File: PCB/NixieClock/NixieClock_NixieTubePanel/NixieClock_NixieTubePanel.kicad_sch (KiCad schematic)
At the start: 31 parts, among them J3 Conn_01x04_Pin, J4 Conn_01x04_Pin, U1 K155ID1, U2 K155ID1, U3 K155ID1, U4 K155ID1, U5 PCF8574, U6 PCF8574, X1 5230, X2 5230, X3 5230, X4 5230, X5 5230, X6 5230

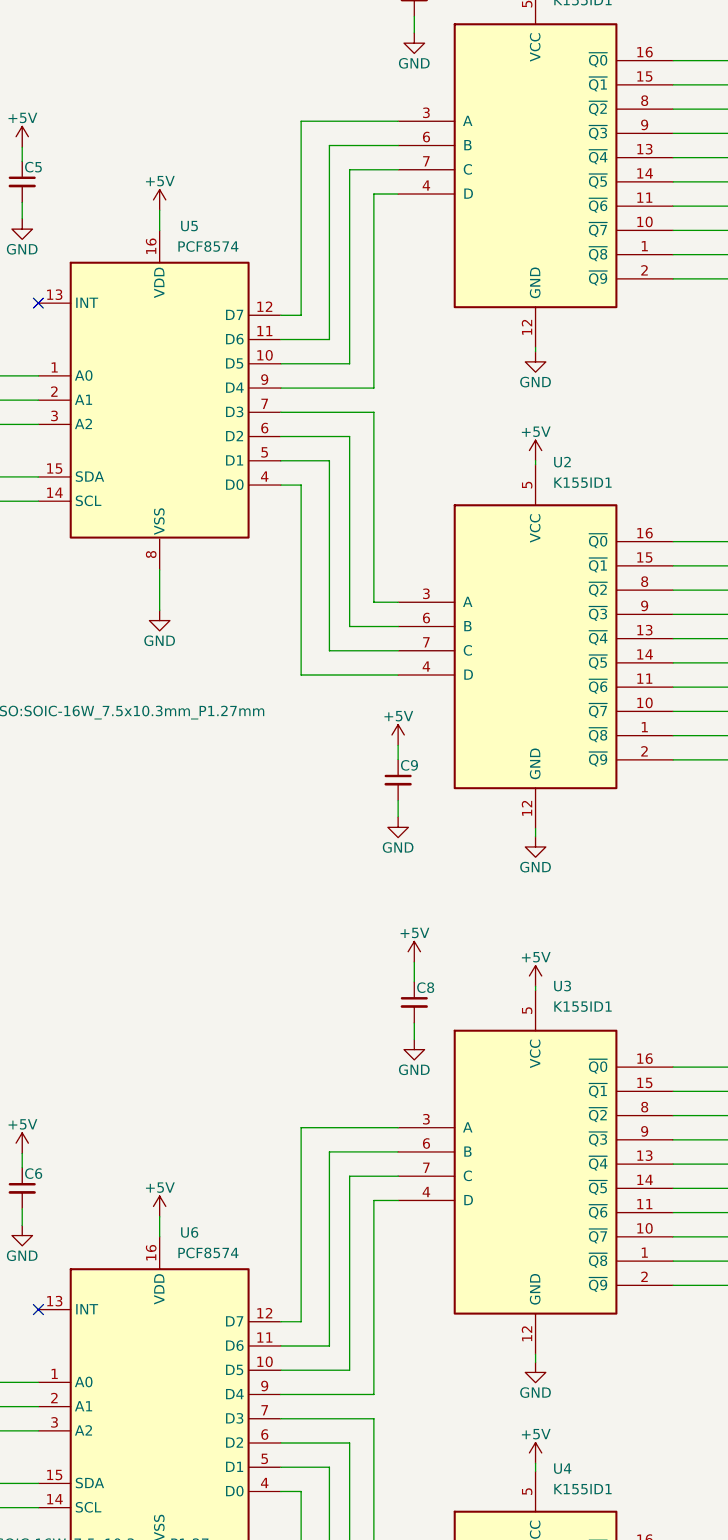
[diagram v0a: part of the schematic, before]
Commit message: Tidied U1 and U3 connections
adjust pin ordering on U1 and U3 in schematic so they would connect to the PCF chips neater on the PCB without needing vias
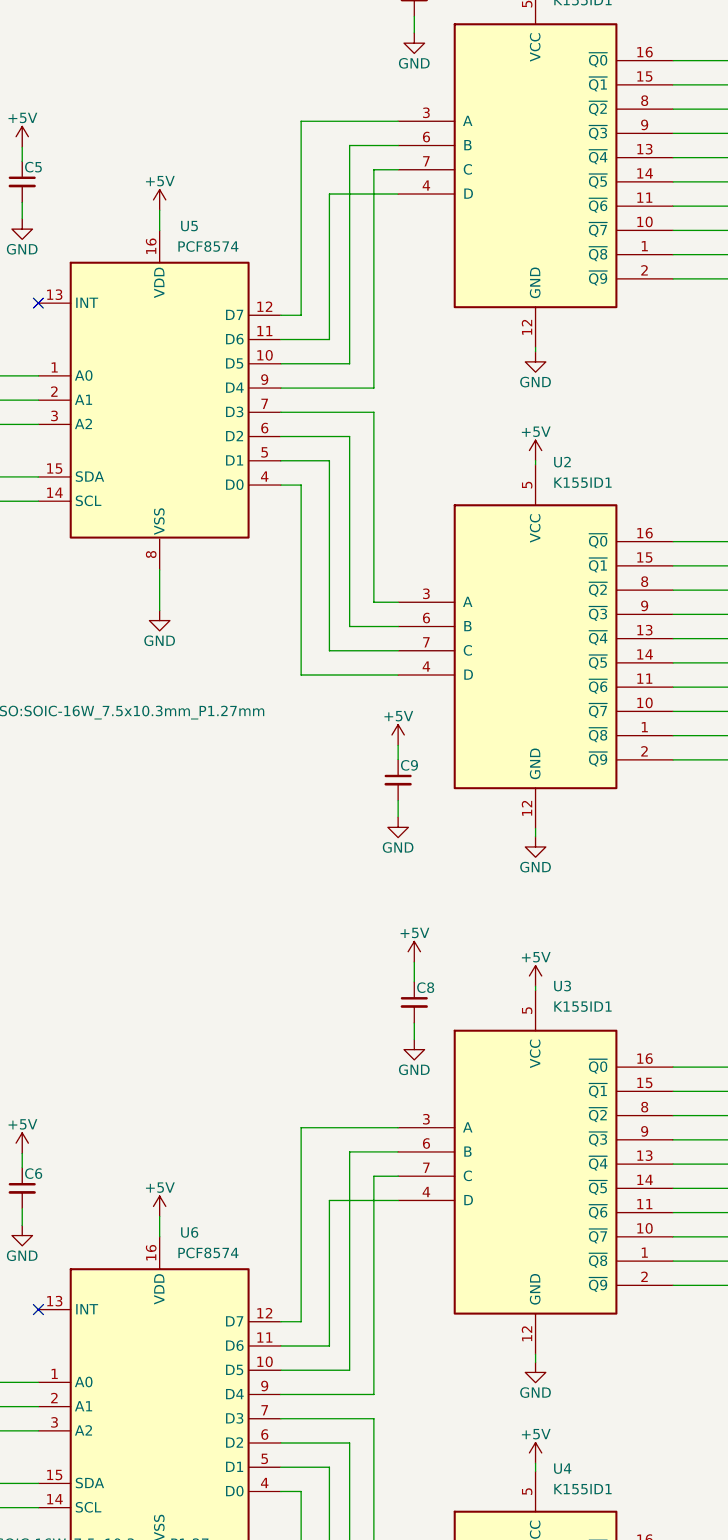
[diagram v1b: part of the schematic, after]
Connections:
- net at U5.10 (D5): now also U1.6 (B); no longer U1.7 (C)
- net at U5.11 (D6): now also U1.4 (D); no longer U1.6 (B)
- net at U5.9 (D4): now also U1.7 (C); no longer U1.4 (D)
- net at U3.4 (D): now also U6.11 (D6); no longer U6.9 (D4)
- net at U3.6 (B): now also U6.10 (D5); no longer U6.11 (D6)
- net at U3.7 (C): now also U6.9 (D4); no longer U6.10 (D5)
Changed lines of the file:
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@@
-	(wire
-		(pts
-			(xy 170 55) (xy 170 79)
-		)
-		(stroke
-			(width 0)
-			(type default)
-		)
-	)
 	(wire
 		(pts
@@
 	(wire
 		(pts
-			(xy 167.5 52) (xy 176 52)
-		)
-		(stroke
-			(width 0)
-			(type default)
-		)
-	)
-	(wire
-		(pts
 			(xy 35 261) (xy 35 262.5)
 		)
@@
 	(wire
 		(pts
-			(xy 173 82) (xy 173 58)
+			(xy 173 55) (xy 173 82)
 		)
 		(stroke
@@
 	(wire
 		(pts
-			(xy 167.5 200.5) (xy 167.5 176.5)
+			(xy 167.5 200.5) (xy 167.5 182.5)
 		)
 		(stroke
@@
 	(wire
 		(pts
+			(xy 170 52) (xy 176 52)
+		)
+		(stroke
+			(width 0)
+			(type default)
+		)
+	)
+	(wire
+		(pts
 			(xy 146.5 60) (xy 146.5 62.5)
 		)
@@
 	(wire
 		(pts
+			(xy 170 176.5) (xy 176 176.5)
+		)
+		(stroke
+			(width 0)
+			(type default)
+		)
+	)
+	(wire
+		(pts
 			(xy 232.5 172) (xy 232.5 164.5)
 		)
@@
 	(wire
 		(pts
-			(xy 167.5 76) (xy 167.5 52)
+			(xy 167.5 76) (xy 167.5 58)
 		)
 		(stroke
@@
 	(wire
 		(pts
-			(xy 170 179.5) (xy 170 203.5)
+			(xy 170 176.5) (xy 170 203.5)
 		)
 		(stroke
@@
 	(wire
 		(pts
+			(xy 176 179.5) (xy 173 179.5)
+		)
+		(stroke
+			(width 0)
+			(type default)
+		)
+	)
+	(wire
+		(pts
 			(xy 260 188) (xy 260 194.5)
 		)
@@
 	(wire
 		(pts
-			(xy 176 179.5) (xy 170 179.5)
-		)
-		(stroke
-			(width 0)
-			(type default)
-		)
-	)
-	(wire
-		(pts
 			(xy 255 251.5) (xy 255 247.5)
 		)
@@
 	(wire
 		(pts
+			(xy 170 52) (xy 170 79)
+		)
+		(stroke
+			(width 0)
+			(type default)
+		)
+	)
+	(wire
+		(pts
 			(xy 235.5 103) (xy 245.5 103)
 		)
@@
 	(wire
 		(pts
-			(xy 173 182.5) (xy 176 182.5)
-		)
-		(stroke
-			(width 0)
-			(type default)
-		)
-	)
-	(wire
-		(pts
 			(xy 69 166.5) (xy 69 160.54)
 		)
@@
 	(wire
 		(pts
-			(xy 173 58) (xy 176 58)
-		)
-		(stroke
-			(width 0)
-			(type default)
-		)
-	)
-	(wire
-		(pts
 			(xy 21 274) (xy 21 275.5)
 		)
@@
 	(wire
 		(pts
+			(xy 167.5 182.5) (xy 176 182.5)
+		)
+		(stroke
+			(width 0)
+			(type default)
+		)
+	)
+	(wire
+		(pts
 			(xy 260 35) (xy 260 43.5)
 		)
@@
 	(wire
 		(pts
+			(xy 173 55) (xy 176 55)
+		)
+		(stroke
+			(width 0)
+			(type default)
+		)
+	)
+	(wire
+		(pts
 			(xy 178 36.04) (xy 178 38.072)
 		)
@@
 	(wire
 		(pts
+			(xy 167.5 58) (xy 176 58)
+		)
+		(stroke
+			(width 0)
+			(type default)
+		)
+	)
+	(wire
+		(pts
 			(xy 43.5 27.54) (xy 43.5 30.19)
 		)
@@
 	(wire
 		(pts
-			(xy 176 55) (xy 170 55)
-		)
-		(stroke
-			(width 0)
-			(type default)
-		)
-	)
-	(wire
-		(pts
 			(xy 173 209.5) (xy 173 233)
 		)
@@
 	(wire
 		(pts
-			(xy 173 206.5) (xy 173 182.5)
+			(xy 173 179.5) (xy 173 206.5)
 		)
 		(stroke
@@
 		)
 		(stroke
-			(width 0)
-			(type default)
-		)
-	)
-	(wire
-		(pts
-			(xy 167.5 176.5) (xy 176 176.5)
-		)
-		(stroke

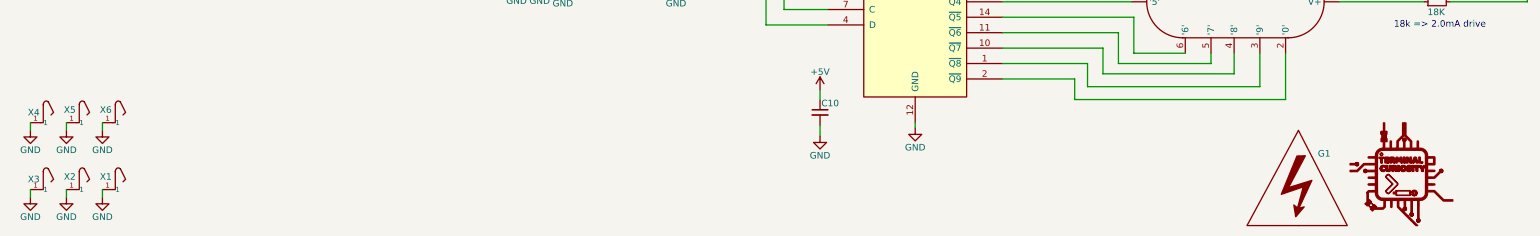
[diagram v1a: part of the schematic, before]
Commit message: DRC cleared
0 DRC errors
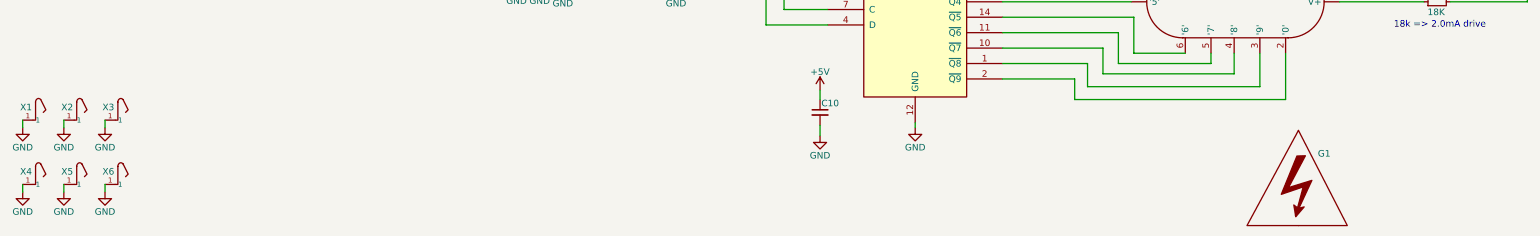
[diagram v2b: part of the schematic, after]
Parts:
- removed G2: LOGO, TerminalCuriosityFootprints:LABEL_TerminalCuriosity_25.0x25.0mm, symbol TerminalCuriosityLogo:LOGO
- N1, N2, N3, N4: footprint TerminalCuriosityFootprints:in-12_nixie-tube -> TerminalCuriosityFootprints:in-12_nixie-tube-socket
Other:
- moved on the sheet: X1

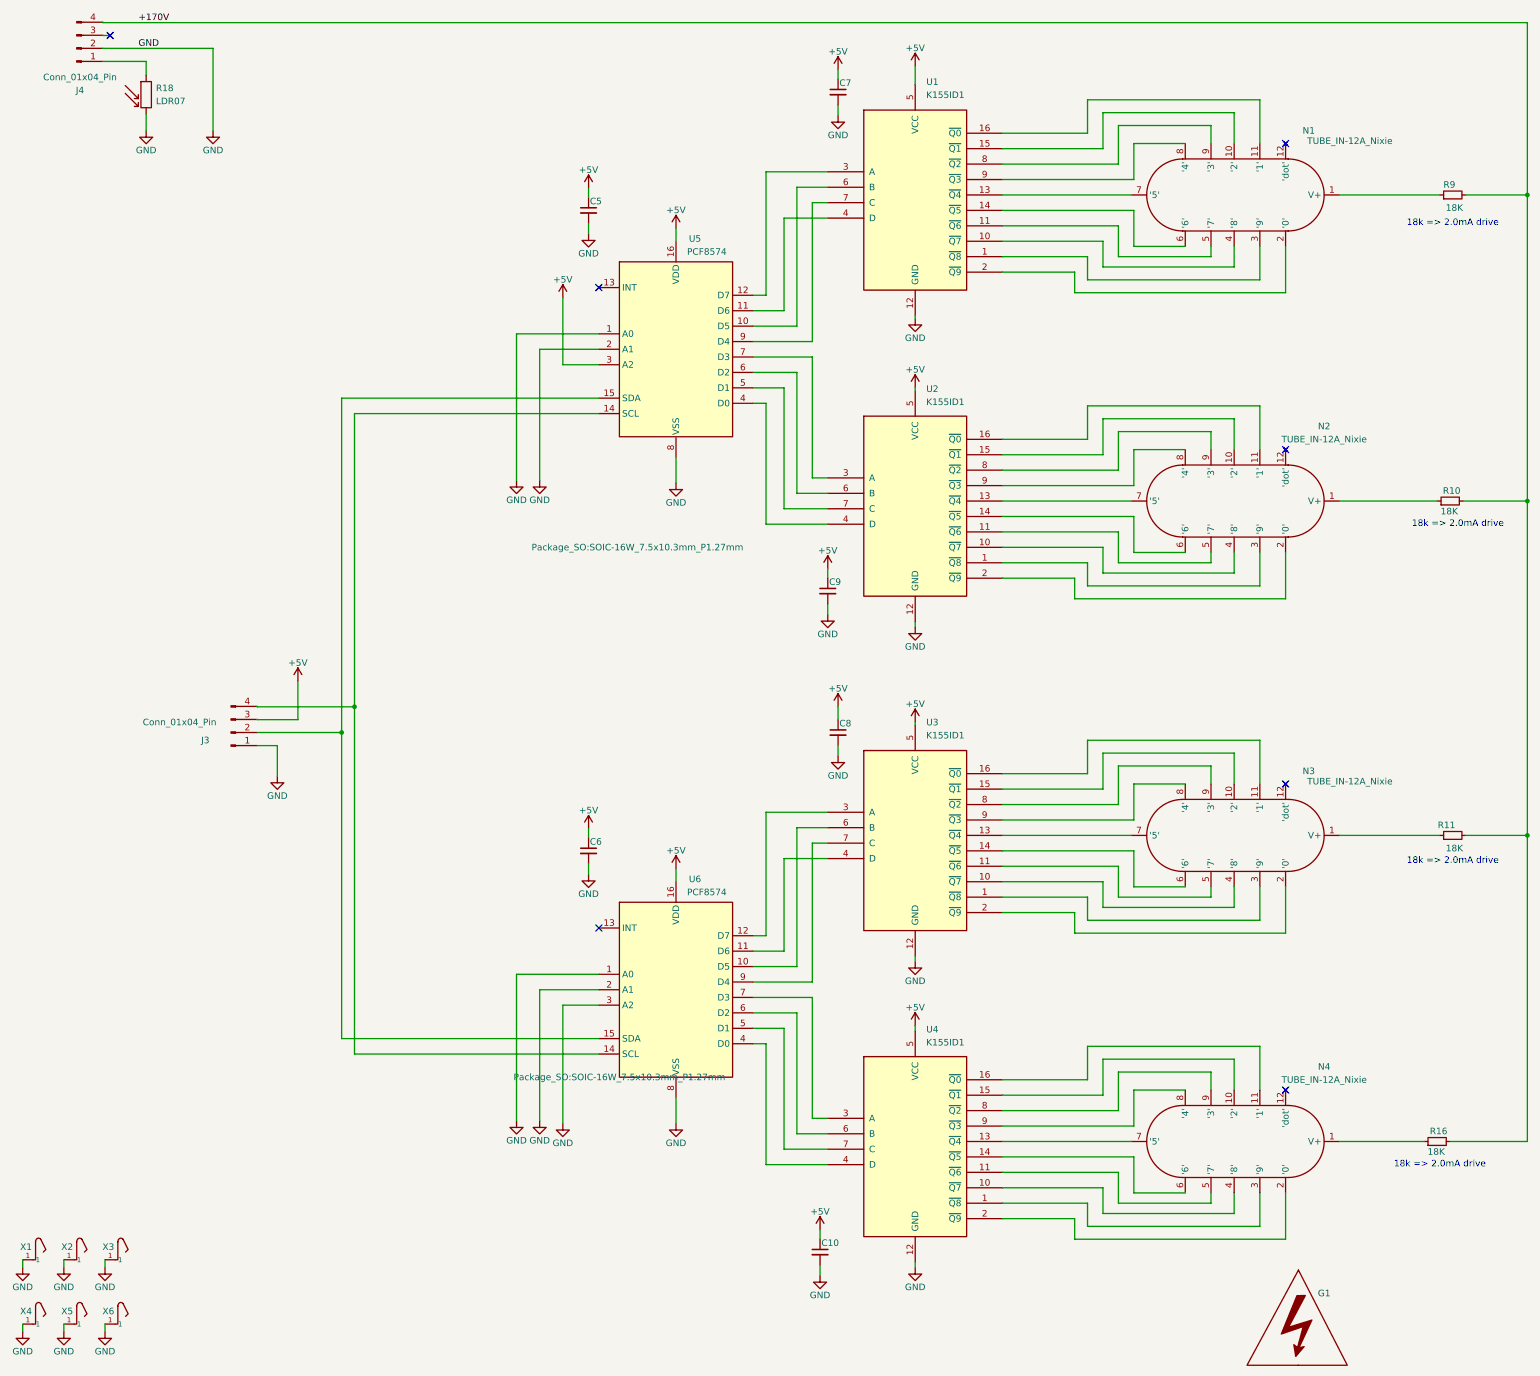
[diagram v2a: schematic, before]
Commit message: Tidy component details and add BOM
fill missing supplier/mfr info on resistors and caps. export BOM
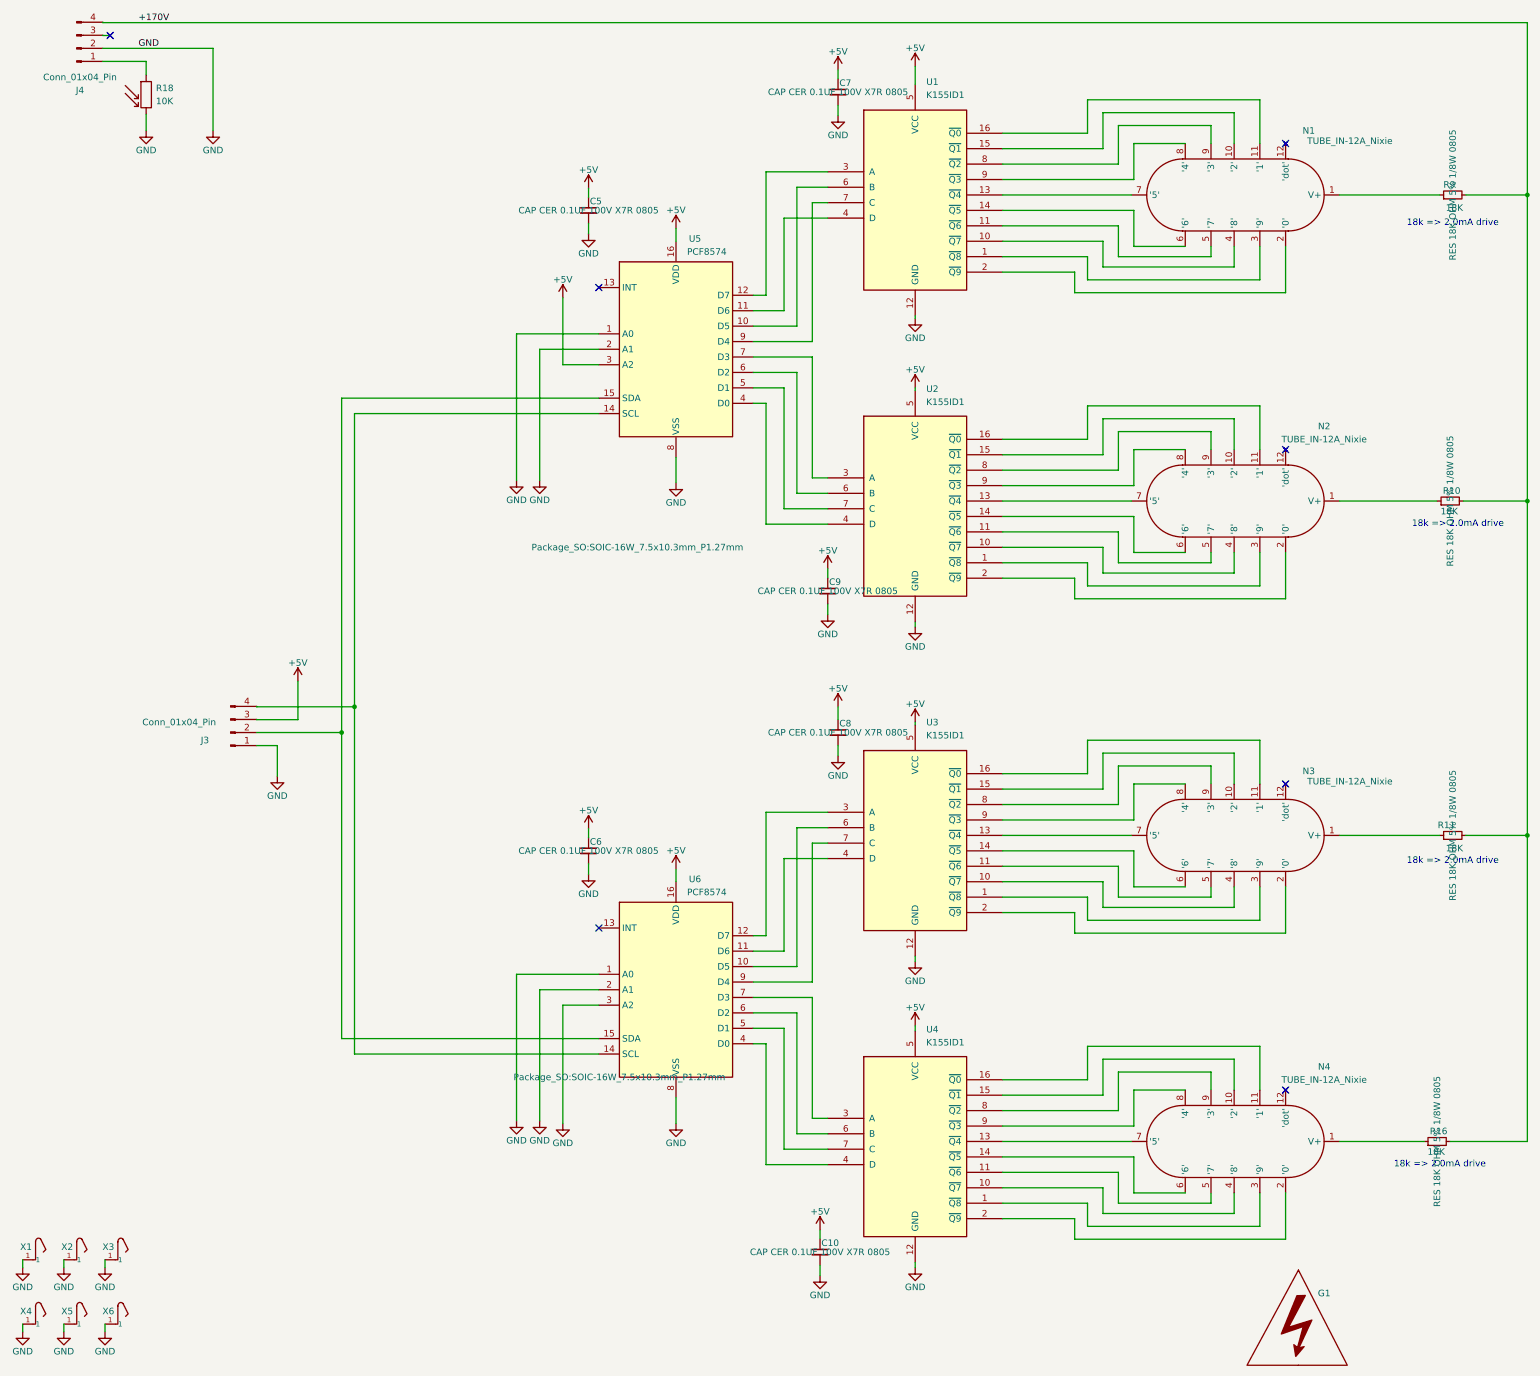
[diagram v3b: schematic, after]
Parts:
- C10, C5, C6, C7, C8, C9: Manufacturer P/N CL21B104KCFNNNE -> (none); Manufacturer PN (none) -> CL21B104KCFNNNE
- J3, J4: Manufacturer (none) -> Wurth Elektronik; Manufacturer PN (none) -> 61300411121; Supplier (none) -> Digikey
- N1, N2, N3, N4, U2, U3, U4: Manufacturer (none) -> Unknown; Manufacturer PN (none) -> Unknown; Supplier (none) -> eBay
- R10, R16: Manufacturer P/N RC0805JR-0718KL -> (none); Manufacturer PN (none) -> RC0805JR-0718KL
- R11, R9: Supplier (none) -> Digikey
- R18: value LDR07 -> 10K; Manufacturer (none) -> LDR Photoresistors; Manufacturer PN (none) -> LDR07; Supplier (none) -> Unknown
- U1: MANUFACTURER MSI -> (none); Manufacturer (none) -> Unknown; Manufacturer PN (none) -> Unknown; Supplier (none) -> eBay
- U5, U6: Manufacturer (none) -> Texas Instruments; Manufacturer PN (none) -> PCF8574ADWR; Supplier (none) -> Digikey
- X1, X2, X3, X4, X5, X6: Manufacturer P/N 122TR -> (none); Manufacturer PN (none) -> 122TR

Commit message: Change anode resistors from 0805 to 1206 for increased power headroom
changed resistors and adjusted traces to suit.
0805 resistors have Pmax 0.125W. if the PSU drifts up to 180-185V, it may exceed this power rating.
1206 doubles the headroom
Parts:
- R10, R11, R16, R9: footprint Resistor_SMD:R_0805_2012Metric_Pad1.20x1.40mm_HandSolder -> Resistor_SMD:R_1206_3216Metric_Pad1.30x1.75mm_HandSolder
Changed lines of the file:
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@@
 			)
 		)
-		(property "Footprint" "Resistor_SMD:R_0805_2012Metric_Pad1.20x1.40mm_HandSolder"
+		(property "Footprint" "Resistor_SMD:R_1206_3216Metric_Pad1.30x1.75mm_HandSolder"
 			(at 294.46 237.5 0)
 			(effects
@@
 			)
 		)
-		(property "Footprint" "Resistor_SMD:R_0805_2012Metric_Pad1.20x1.40mm_HandSolder"
+		(property "Footprint" "Resistor_SMD:R_1206_3216Metric_Pad1.30x1.75mm_HandSolder"
 			(at 297.5 178 0)
 			(effects
@@
 				)
 				(hide yes)
+			)
+		)
+		(property "Company" ""
+			(at 297.5 178 0)
+			(effects
+				(font
+					(size 1.27 1.27)
+				)
 			)
 		)
@@
 			)
 		)
-		(property "Footprint" "Resistor_SMD:R_0805_2012Metric_Pad1.20x1.40mm_HandSolder"
+		(property "Footprint" "Resistor_SMD:R_1206_3216Metric_Pad1.30x1.75mm_HandSolder"
 			(at 297.5 53.5 0)
 			(effects
@@
 			)
 		)
+		(property "Company" ""
+			(at 297.5 53.5 0)
+			(effects
+				(font
+					(size 1.27 1.27)
+				)
+			)
+		)
 		(pin "1"
 		)
@@
 			)
 		)
-		(property "Footprint" "Resistor_SMD:R_0805_2012Metric_Pad1.20x1.40mm_HandSolder"
+		(property "Footprint" "Resistor_SMD:R_1206_3216Metric_Pad1.30x1.75mm_HandSolder"
 			(at 297 113 0)
 			(effects
